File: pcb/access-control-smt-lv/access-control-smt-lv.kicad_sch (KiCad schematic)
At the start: 25 parts, among them U1 ESP32-WROOM-E

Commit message: Mostly done SMT controller
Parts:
- added C1: 0.1U, Capacitor_SMD:C_1808_4520Metric_Pad1.72x2.30mm_HandSolder, symbol Device:C
- added CON_3v3, CON_5v1: Conn_01x02_Socket, Connector_PinHeader_2.54mm:PinHeader_1x02_P2.54mm_Vertical, symbol Connector:Conn_01x02_Socket
- added CON_AUX1: Conn_01x04_Socket, Connector_PinHeader_2.54mm:PinHeader_1x04_P2.54mm_Vertical, symbol Connector:Conn_01x04_Socket
- added R_EN1: 10kR, Resistor_SMD:R_2010_5025Metric_Pad1.40x2.65mm_HandSolder, symbol Device:R
- PAD_SWL1, PAD_SWS1: footprint Connector_Wire:SolderWirePad_1x01_SMD_5x10mm -> Connector_Wire:SolderWirePad_1x01_SMD_1x2mm
- R_BUTTON_PD1: footprint Resistor_SMD:R_2816_7142Metric_Pad3.20x4.45mm_HandSolder -> Resistor_SMD:R_2010_5025Metric_Pad1.40x2.65mm_HandSolder
- R_LED1: renamed from R_LED; footprint Resistor_SMD:R_2816_7142Metric_Pad3.20x4.45mm_HandSolder -> Resistor_SMD:R_2010_5025Metric_Pad1.40x2.65mm_HandSolder
- R_Q_LED1: renamed from R_Q_LED; footprint Resistor_SMD:R_2816_7142Metric_Pad3.20x4.45mm_HandSolder -> Resistor_SMD:R_2010_5025Metric_Pad1.40x2.65mm_HandSolder
- R_Q_RELAY1: renamed from R_Q_RELAY; footprint Resistor_SMD:R_2816_7142Metric_Pad3.20x4.45mm_HandSolder -> Resistor_SMD:R_2010_5025Metric_Pad1.40x2.65mm_HandSolder
- renumbered C_PWR_5V to C_PWR_5V1, D_Z_5V to D_Z_5V1, J_LED to J_LED1, J_NFC to J_NFC1, J_RELAY to J_RELAY1, J_SERIAL to J_SERIAL1, Q_LED to Q_LED1, Q_RELAY to Q_RELAY1, SW_BOOT to SW_BOOT1, SW_RESET to SW_RESET1
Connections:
- net +3V3: now also CON_3v3.1 (Pin_1), CON_AUX1.1 (Pin_1), R_EN1.1
- net +5V: now also CON_5v1.1 (Pin_1)
- net GND: now also C1.2, CON_3v3.2 (Pin_2), CON_5v1.2 (Pin_2), CON_AUX1.2 (Pin_2)
- net at SW_RESET1.2, U1.3 (EN/CHIP_PU): now also C1.1, R_EN1.2
- net at U1.8 (32K_XP/GPIO32/ADC1_CH4): now also CON_AUX1.4 (Pin_4)
- net at U1.9 (32K_XN/GPIO33/ADC1_CH5): now also CON_AUX1.3 (Pin_3)
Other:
- moved on the sheet: SW_RESET1

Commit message: NFC Clamp and progress with contactor interface
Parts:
- C_PWR_3v3, C_PWR_5V1: footprint Capacitor_SMD:C_1808_4520Metric_Pad1.72x2.30mm_HandSolder -> Capacitor_SMD:C_1812_4532Metric_Pad1.57x3.40mm_HandSolder
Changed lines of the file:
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@@
 		(dnp no)
 		(fields_autoplaced yes)
-		(property "Reference" "#PWR25"
+		(property "Reference" "#PWR025"
 			(at 49.53 106.68 0)
 			(effects
@@
 			(project ""
 				(path "/7cf59121-d90a-405f-864e-dd3e48ad3dc1"
-					(reference "#PWR25")
+					(reference "#PWR025")
 					(unit 1)
 				)
@@
 		(dnp no)
 		(fields_autoplaced yes)
-		(property "Reference" "#PWR26"
+		(property "Reference" "#PWR026"
 			(at 49.53 111.76 0)
 			(effects
@@
 			(project ""
 				(path "/7cf59121-d90a-405f-864e-dd3e48ad3dc1"
-					(reference "#PWR26")
+					(reference "#PWR026")
 					(unit 1)
 				)
@@
 			)
 		)
-		(property "Footprint" "Capacitor_SMD:C_1808_4520Metric_Pad1.72x2.30mm_HandSolder"
+		(property "Footprint" "Capacitor_SMD:C_1812_4532Metric_Pad1.57x3.40mm_HandSolder"
 			(at 47.9552 34.29 0)
 			(effects
@@
 		(dnp no)
 		(fields_autoplaced yes)
-		(property "Reference" "#PWR28"
+		(property "Reference" "#PWR028"
 			(at 44.45 62.23 0)
 			(effects
@@
 			(project "access-control-smt-lv"
 				(path "/7cf59121-d90a-405f-864e-dd3e48ad3dc1"
-					(reference "#PWR28")
+					(reference "#PWR028")
 					(unit 1)
 				)
@@
 			)
 		)
-		(property "Footprint" "Capacitor_SMD:C_1808_4520Metric_Pad1.72x2.30mm_HandSolder"
+		(property "Footprint" "Capacitor_SMD:C_1812_4532Metric_Pad1.57x3.40mm_HandSolder"
 			(at 17.4752 34.29 0)
 			(effects
@@
 		(dnp no)
 		(fields_autoplaced yes)
-		(property "Reference" "#PWR29"
+		(property "Reference" "#PWR029"
 			(at 77.47 121.92 0)
 			(effects
@@
 			(project "access-control-smt-lv"
 				(path "/7cf59121-d90a-405f-864e-dd3e48ad3dc1"
-					(reference "#PWR29")
+					(reference "#PWR029")
 					(unit 1)
 				)
@@
 		(dnp no)
 		(fields_autoplaced yes)
-		(property "Reference" "#PWR30"
+		(property "Reference" "#PWR030"
 			(at 77.47 128.27 0)
 			(effects
@@
 			(project "access-control-smt-lv"
 				(path "/7cf59121-d90a-405f-864e-dd3e48ad3dc1"
-					(reference "#PWR30")
+					(reference "#PWR030")
 					(unit 1)
 				)
@@
 		(dnp no)
 		(fields_autoplaced yes)
-		(property "Reference" "#PWR27"
+		(property "Reference" "#PWR027"
 			(at 39.37 67.31 0)
 			(effects
@@
 			(project "access-control-smt-lv"
 				(path "/7cf59121-d90a-405f-864e-dd3e48ad3dc1"
-					(reference "#PWR27")
+					(reference "#PWR027")
 					(unit 1)
 				)
@@
 		(dnp no)
 		(fields_autoplaced yes)
-		(property "Reference" "#PWR24"
+		(property "Reference" "#PWR024"
 			(at 13.97 49.53 0)
 			(effects
@@
 			(project ""
 				(path "/7cf59121-d90a-405f-864e-dd3e48ad3dc1"
-					(reference "#PWR24")
-					(unit 1)
-				)
+					(reference "#PWR024")
+					(unit 1)
+				)

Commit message: Further optimisation of SMT version
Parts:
- C3: footprint Capacitor_SMD:C_1808_4520Metric_Pad1.72x2.30mm_HandSolder -> Capacitor_SMD:C_1206_3216Metric_Pad1.33x1.80mm_HandSolder
- C_PWR_3v3, C_PWR_5V1: footprint Capacitor_SMD:C_1812_4532Metric_Pad1.57x3.40mm_HandSolder -> Capacitor_SMD:C_1206_3216Metric_Pad1.33x1.80mm_HandSolder
- D_Z_3v3: footprint Diode_SMD:D_1210_3225Metric_Pad1.42x2.65mm_HandSolder -> Diode_SMD:D_0805_2012Metric_Pad1.15x1.40mm_HandSolder
- D_Z_5V1: footprint Diode_SMD:D_1210_3225Metric_Pad1.42x2.65mm_HandSolder -> Diode_SMD:D_1206_3216Metric_Pad1.42x1.75mm_HandSolder
- R_BUTTON_PD1, R_EN1, R_LED1, R_Q_LED1, R_Q_RELAY1: footprint Resistor_SMD:R_2010_5025Metric_Pad1.40x2.65mm_HandSolder -> Resistor_SMD:R_1206_3216Metric_Pad1.30x1.75mm_HandSolder
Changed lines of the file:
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@@
 			)
 		)
-		(property "Footprint" "Resistor_SMD:R_2010_5025Metric_Pad1.40x2.65mm_HandSolder"
+		(property "Footprint" "Resistor_SMD:R_1206_3216Metric_Pad1.30x1.75mm_HandSolder"
 			(at 163.322 31.75 90)
 			(effects
@@
 			)
 		)
-		(property "Footprint" "Capacitor_SMD:C_1812_4532Metric_Pad1.57x3.40mm_HandSolder"
+		(property "Footprint" "Capacitor_SMD:C_1206_3216Metric_Pad1.33x1.80mm_HandSolder"
 			(at 47.9552 34.29 0)
 			(effects
@@
 			)
 		)
-		(property "Footprint" "Capacitor_SMD:C_1812_4532Metric_Pad1.57x3.40mm_HandSolder"
+		(property "Footprint" "Capacitor_SMD:C_1206_3216Metric_Pad1.33x1.80mm_HandSolder"
 			(at 17.4752 34.29 0)
 			(effects
@@
 			)
 		)
-		(property "Footprint" "Resistor_SMD:R_2010_5025Metric_Pad1.40x2.65mm_HandSolder"
+		(property "Footprint" "Resistor_SMD:R_1206_3216Metric_Pad1.30x1.75mm_HandSolder"
 			(at 12.192 52.07 90)
 			(effects
@@
 			)
 		)
-		(property "Footprint" "Capacitor_SMD:C_1808_4520Metric_Pad1.72x2.30mm_HandSolder"
+		(property "Footprint" "Capacitor_SMD:C_1206_3216Metric_Pad1.33x1.80mm_HandSolder"
 			(at 68.2752 30.48 0)
 			(effects
@@
 			)
 		)
-		(property "Footprint" "Resistor_SMD:R_2010_5025Metric_Pad1.40x2.65mm_HandSolder"
+		(property "Footprint" "Resistor_SMD:R_1206_3216Metric_Pad1.30x1.75mm_HandSolder"
 			(at 190.5 109.728 90)
 			(effects
@@
 			)
 		)
-		(property "Footprint" "Resistor_SMD:R_2010_5025Metric_Pad1.40x2.65mm_HandSolder"
+		(property "Footprint" "Resistor_SMD:R_1206_3216Metric_Pad1.30x1.75mm_HandSolder"
 			(at 190.5 62.738 90)
 			(effects
@@
 			)
 		)
-		(property "Footprint" "Diode_SMD:D_1210_3225Metric_Pad1.42x2.65mm_HandSolder"
+		(property "Footprint" "Diode_SMD:D_0805_2012Metric_Pad1.15x1.40mm_HandSolder"
 			(at 105.41 30.48 0)
 			(effects
@@
 			)
 		)
-		(property "Footprint" "Diode_SMD:D_1210_3225Metric_Pad1.42x2.65mm_HandSolder"
+		(property "Footprint" "Diode_SMD:D_1206_3216Metric_Pad1.42x1.75mm_HandSolder"
 			(at 22.86 30.48 0)
 			(effects
@@
 			)
 		)
-		(property "Footprint" "Resistor_SMD:R_2010_5025Metric_Pad1.40x2.65mm_HandSolder"
+		(property "Footprint" "Resistor_SMD:R_1206_3216Metric_Pad1.30x1.75mm_HandSolder"
 			(at 218.44 56.388 90)
 			(effects

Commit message: SMT PCB Updates
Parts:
- added CON_5v2: Conn_01x02_Socket, Connector_PinHeader_2.54mm:PinHeader_1x02_P2.54mm_Vertical, symbol Connector:Conn_01x02_Socket
- added R_PRGM_SERIAL1: 10kR, Resistor_SMD:R_1206_3216Metric_Pad1.30x1.75mm_HandSolder, symbol Device:R
- C1: footprint Capacitor_SMD:C_1808_4520Metric_Pad1.72x2.30mm_HandSolder -> Capacitor_SMD:C_1206_3216Metric_Pad1.33x1.80mm_HandSolder
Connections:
- net +5V: now also CON_5v2.1 (Pin_1)
- net GND: now also CON_5v2.2 (Pin_2), R_PRGM_SERIAL1.2
- net at U1.24 (ADC2_CH2/GPIO2): now also R_PRGM_SERIAL1.1

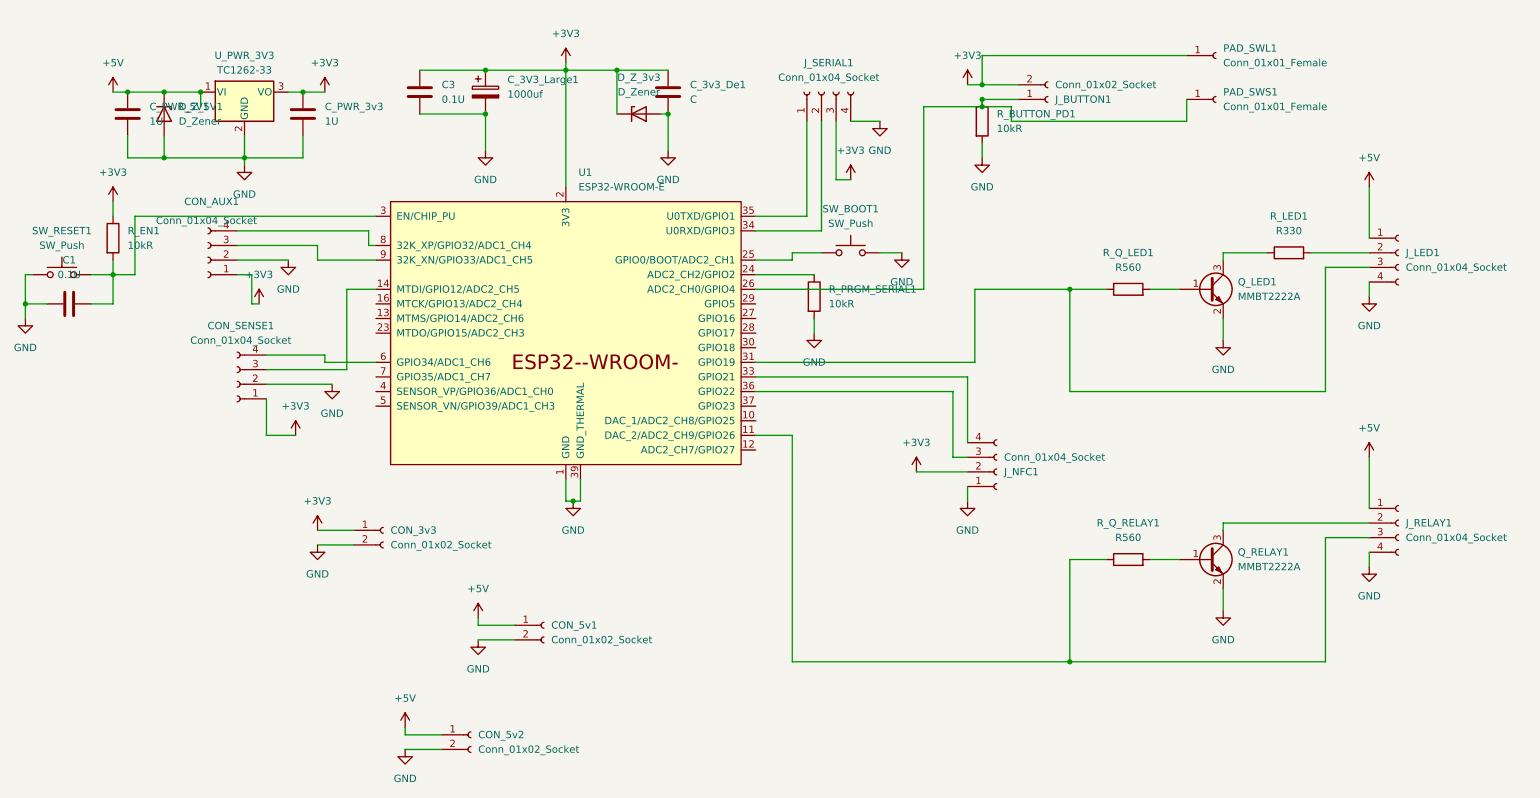
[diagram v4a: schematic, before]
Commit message: Fixes to relief, JST connectors for SMT board
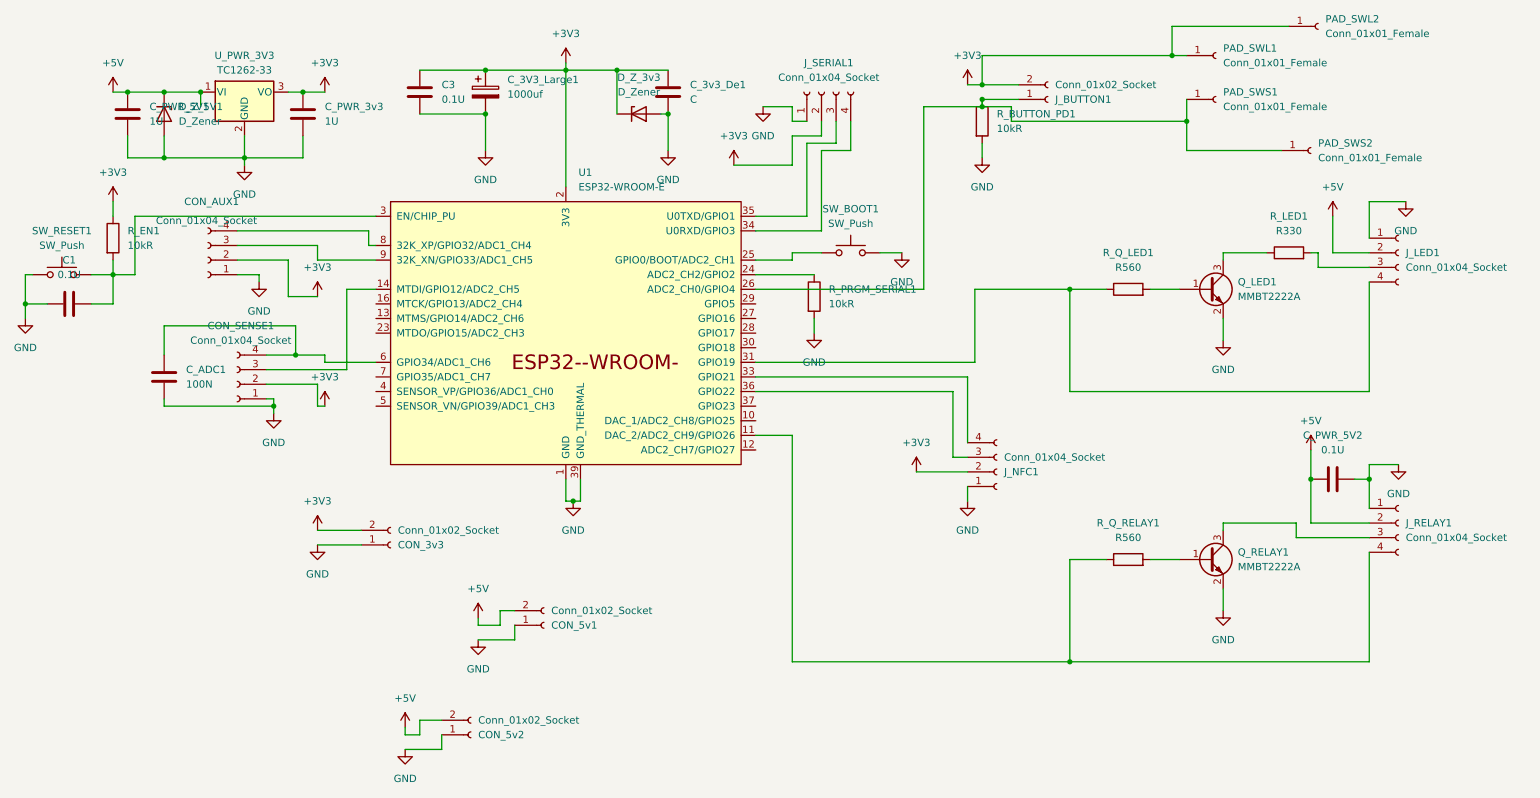
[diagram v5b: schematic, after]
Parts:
- added C_ADC1: 100N, Capacitor_SMD:C_1206_3216Metric_Pad1.33x1.80mm_HandSolder, symbol Device:C
- added C_PWR_5V2: 0.1U, Capacitor_SMD:C_1206_3216Metric_Pad1.33x1.80mm_HandSolder, symbol Device:C
- added PAD_SWL2, PAD_SWS2: Conn_01x01_Female, Connector_Wire:SolderWirePad_1x01_SMD_1x2mm, symbol Connector:Conn_01x01_Female
- CON_5v2: footprint Connector_PinHeader_2.54mm:PinHeader_1x02_P2.54mm_Vertical -> Connector_JST:JST_XH_B2B-XH-A_1x02_P2.50mm_Vertical
- CON_SENSE1: footprint Connector_PinHeader_2.54mm:PinHeader_1x04_P2.54mm_Vertical -> Connector_JST:JST_XH_B4B-XH-A_1x04_P2.50mm_Vertical
- J_NFC1, J_RELAY1, J_SERIAL1: footprint Connector_PinSocket_2.54mm:PinSocket_1x04_P2.54mm_Vertical -> Connector_JST:JST_XH_B4B-XH-A_1x04_P2.50mm_Vertical
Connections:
- net +3V3: now also CON_3v3.2 (Pin_2), CON_AUX1.2 (Pin_2), CON_SENSE1.2 (Pin_2), J_SERIAL1.2 (Pin_2), PAD_SWL2.1 (Pin_1); no longer CON_3v3.1 (Pin_1), CON_AUX1.1 (Pin_1), CON_SENSE1.1 (Pin_1), J_SERIAL1.3 (Pin_3)
- net +5V: now also CON_5v1.2 (Pin_2), CON_5v2.2 (Pin_2), J_LED1.2 (Pin_2), J_RELAY1.2 (Pin_2), C_PWR_5V2.1; no longer CON_5v1.1 (Pin_1), CON_5v2.1 (Pin_1), J_LED1.1 (Pin_1), J_RELAY1.1 (Pin_1)
- net GND: now also CON_3v3.1 (Pin_1), CON_5v1.1 (Pin_1), CON_5v2.1 (Pin_1), CON_AUX1.1 (Pin_1), CON_SENSE1.1 (Pin_1), J_LED1.1 (Pin_1), J_RELAY1.1 (Pin_1), J_SERIAL1.1 (Pin_1), C_ADC1.2, C_PWR_5V2.2; no longer CON_3v3.2 (Pin_2), CON_5v1.2 (Pin_2), CON_5v2.2 (Pin_2), CON_AUX1.2 (Pin_2), CON_SENSE1.2 (Pin_2), J_LED1.4 (Pin_4), J_RELAY1.4 (Pin_4), J_SERIAL1.4 (Pin_4)
- net at J_BUTTON1.1 (Pin_1), PAD_SWS1.1 (Pin_1), R_BUTTON_PD1.1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: now also PAD_SWS2.1 (Pin_1)
- net at CON_SENSE1.4 (Pin_4), U1.6 (GPIO34/ADC1_CH6): now also C_ADC1.1
- net at Q_RELAY1.3 (C): now also J_RELAY1.3 (Pin_3); no longer J_RELAY1.2 (Pin_2)
- net at U1.35 (U0TXD/GPIO1): now also J_SERIAL1.3 (Pin_3); no longer J_SERIAL1.1 (Pin_1)
- net at U1.34 (U0RXD/GPIO3): now also J_SERIAL1.4 (Pin_4); no longer J_SERIAL1.2 (Pin_2)
- net at R_Q_RELAY1.1, U1.11 (DAC_2/ADC2_CH9/GPIO26): now also J_RELAY1.4 (Pin_4); no longer J_RELAY1.3 (Pin_3)
- net at R_Q_LED1.1, U1.31 (GPIO19): now also J_LED1.4 (Pin_4); no longer J_LED1.3 (Pin_3)
- net at R_LED1.2: now also J_LED1.3 (Pin_3); no longer J_LED1.2 (Pin_2)
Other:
- moved on the sheet: CON_3v3, CON_5v1, CON_5v2

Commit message: Silkscreen updates with version, date and logo
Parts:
- renumbered CON_5v2 to CON_5v1, J_NFC1 to CON_NFC1, J_RELAY1 to CON_RELAY1, CON_3v3 to J_3v3, CON_5v1 to J_5v1
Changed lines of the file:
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@@
 		(on_board yes)
 		(dnp no)
-		(property "Reference" "CON_3v3"
+		(property "Reference" "J_3v3"
 			(at 63.5 105.4101 0)
 			(effects
@@
 			(project ""
 				(path "/7cf59121-d90a-405f-864e-dd3e48ad3dc1"
-					(reference "CON_3v3")
+					(reference "J_3v3")
 					(unit 1)
 				)
@@
 		(on_board yes)
 		(dnp no)
-		(property "Reference" "J_NFC1"
+		(property "Reference" "CON_NFC1"
 			(at 168.91 92.7101 0)
 			(effects
@@
 			(project "access-control-smt-lv"
 				(path "/7cf59121-d90a-405f-864e-dd3e48ad3dc1"
-					(reference "J_NFC1")
+					(reference "CON_NFC1")
 					(unit 1)
 				)
@@
 		(on_board yes)
 		(dnp no)
-		(property "Reference" "CON_5v1"
+		(property "Reference" "J_5v1"
 			(at 90.17 119.3801 0)
 			(effects
@@
 			(project "access-control-smt-lv"
 				(path "/7cf59121-d90a-405f-864e-dd3e48ad3dc1"
-					(reference "CON_5v1")
+					(reference "J_5v1")
 					(unit 1)
 				)
@@
 		(on_board yes)
 		(dnp no)
-		(property "Reference" "CON_5v2"
+		(property "Reference" "CON_5v1"
 			(at 77.47 138.4301 0)
 			(effects
@@
 			(project "access-control-smt-lv"
 				(path "/7cf59121-d90a-405f-864e-dd3e48ad3dc1"
-					(reference "CON_5v2")
+					(reference "CON_5v1")
 					(unit 1)
 				)
@@
 		(dnp no)
 		(fields_autoplaced yes)
-		(property "Reference" "J_RELAY1"
+		(property "Reference" "CON_RELAY1"
 			(at 238.76 101.5999 0)
 			(effects
@@
 			(project ""
 				(path "/7cf59121-d90a-405f-864e-dd3e48ad3dc1"
-					(reference "J_RELAY1")
+					(reference "CON_RELAY1")
 					(unit 1)
 				)

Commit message: Final changes pre manufacture
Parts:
- added R_I2C_PU1, R_I2C_PU2: 10kR, Resistor_SMD:R_1206_3216Metric_Pad1.30x1.75mm_HandSolder, symbol Device:R
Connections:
- net +3V3: now also R_I2C_PU1.2, R_I2C_PU2.2
- net at CON_NFC1.3 (Pin_3), U1.36 (GPIO22): now also R_I2C_PU1.1
- net at CON_NFC1.4 (Pin_4), U1.33 (GPIO21): now also R_I2C_PU2.1
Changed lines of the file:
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@@
 	)
 	(junction
+		(at 137.16 76.2)
+		(diameter 0)
+		(color 0 0 0 0)
+	)
+	(junction
 		(at 200.66 31.75)
 		(diameter 0)
@@
 	)
 	(junction
+		(at 144.78 92.71)
+		(diameter 0)
+		(color 0 0 0 0)
+	)
+	(junction
 		(at 198.12 20.32)
 		(diameter 0)
@@
 	)
 	(junction
+		(at 144.78 78.74)
+		(diameter 0)
+		(color 0 0 0 0)
+	)
+	(junction
 		(at 92.71 22.86)
 		(diameter 0)
@@
 	)
 	(junction
+		(at 137.16 92.71)
+		(diameter 0)
+		(color 0 0 0 0)
+	)
+	(junction
 		(at 222.25 93.98)
 		(diameter 0)
@@
 	(wire
 		(pts
+			(xy 137.16 76.2) (xy 162.56 76.2)
+		)
+		(stroke
+			(width 0)
+			(type default)
+		)
+	)
+	(wire
+		(pts
 			(xy 49.53 62.23) (xy 44.45 62.23)
 		)
@@
 	(wire
 		(pts
+			(xy 144.78 92.71) (xy 162.56 92.71)
+		)
+		(stroke
+			(width 0)
+			(type default)
+		)
+	)
+	(wire
+		(pts
 			(xy 22.86 81.28) (xy 41.91 81.28)
 		)
@@
 	(wire
 		(pts
-			(xy 125.73 86.36) (xy 132.08 86.36)
+			(xy 125.73 86.36) (xy 129.54 86.36)
 		)
 		(stroke
@@
 	(wire
 		(pts
+			(xy 137.16 92.71) (xy 144.78 92.71)
+		)
+		(stroke
+			(width 0)
+			(type default)
+		)
+	)
+	(wire
+		(pts
 			(xy 101.6 30.48) (xy 101.6 22.86)
 		)
@@
 	(wire
 		(pts
-			(xy 125.73 76.2) (xy 162.56 76.2)
+			(xy 125.73 76.2) (xy 137.16 76.2)
 		)
 		(stroke
@@
 	(wire
 		(pts
-			(xy 132.08 125.73) (xy 180.34 125.73)
+			(xy 144.78 78.74) (xy 160.02 78.74)
+		)
+		(stroke
+			(width 0)
+			(type default)
+		)
+	)
+	(wire
+		(pts
+			(xy 129.54 125.73) (xy 180.34 125.73)
 		)
 		(stroke
@@
 	(wire
 		(pts
-			(xy 132.08 86.36) (xy 132.08 125.73)
+			(xy 129.54 86.36) (xy 129.54 125.73)
 		)
 		(stroke
@@
 	(wire
 		(pts
-			(xy 153.67 92.71) (xy 162.56 92.71)
+			(xy 134.62 92.71) (xy 137.16 92.71)
 		)
 		(stroke
@@
 	(wire
 		(pts
+			(xy 137.16 83.82) (xy 137.16 92.71)
+		)
+		(stroke
+			(width 0)
+			(type default)
+		)
+	)
+	(wire
+		(pts
 			(xy 22.86 67.31) (xy 22.86 72.39)
 		)
@@
 	(wire
 		(pts
-			(xy 125.73 78.74) (xy 160.02 78.74)
+			(xy 125.73 78.74) (xy 144.78 78.74)
 		)
 		(stroke
@@
 	(wire
 		(pts
+			(xy 144.78 86.36) (xy 144.78 92.71)
+		)
+		(stroke
+			(width 0)
+			(type default)
+		)
+	)
+	(wire
+		(pts
 			(xy 50.8 72.39) (xy 45.72 72.39)
 		)
@@
 	(symbol
 		(lib_id "power:+3V3")
-		(at 153.67 92.71 0)
+		(at 134.62 92.71 0)
 		(unit 1)
 		(exclude_from_sim no)
@@
 		(fields_autoplaced yes)
 		(property "Reference" "#PWR010"
-			(at 153.67 96.52 0)
+			(at 134.62 96.52 0)
 			(effects
 				(font
@@
 		)
 		(property "Value" "+3V3"
-			(at 153.67 87.63 0)
+			(at 134.62 87.63 0)
 			(effects
 				(font
@@
 		)
 		(property "Footprint" ""
-			(at 153.67 92.71 0)
+			(at 134.62 92.71 0)
 			(effects
 				(font
@@
 		)
 		(property "Datasheet" ""
-			(at 153.67 92.71 0)
+			(at 134.62 92.71 0)
 			(effects
 				(font
@@
 		)
 		(property "Description" "Power symbol creates a global label with name \"+3V3\""
-			(at 153.67 92.71 0)
+			(at 134.62 92.71 0)
 			(effects
 				(font
@@
 	)
 	(symbol
+		(lib_id "Device:R")
+		(at 144.78 82.55 0)
+		(unit 1)
+		(exclude_from_sim no)
+		(in_bom yes)
+		(on_board yes)
+		(dnp no)
+		(fields_autoplaced yes)
+		(property "Reference" "R_I2C_PU1"
+			(at 147.32 81.2799 0)
+			(effects
+				(font
+					(size 1.27 1.27)
+				)
+				(justify left)
+			)
+		)
+		(property "Value" "10kR"
+			(at 147.32 83.8199 0)
+			(effects
+				(font
+					(size 1.27 1.27)
+				)
+				(justify left)
+			)
+		)
+		(property "Footprint" "Resistor_SMD:R_1206_3216Metric_Pad1.30x1.75mm_HandSolder"
+			(at 143.002 82.55 90)
+			(effects
+				(font
+					(size 1.27 1.27)
+				)
+				(hide yes)
+			)
+		)
+		(property "Datasheet" "~"
+			(at 144.78 82.55 0)
+			(effects
+				(font
+					(size 1.27 1.27)
+				)
+				(hide yes)
+			)
+		)
+		(property "Description" "Resistor"
+			(at 144.78 82.55 0)
+			(effects
+				(font
+					(size 1.27 1.27)
+				)
+				(hide yes)
+			)
+		)
+		(pin "1"
+		)
+		(pin "2"
+		)
+		(instances
+			(project "access-control-smt-lv"
+				(path "/7cf59121-d90a-405f-864e-dd3e48ad3dc1"
+					(reference "R_I2C_PU1")
+					(unit 1)
+				)
+			)
+		)
+	)
+	(symbol
 		(lib_id "Transistor_BJT:MMBT2222A")
 		(at 204.47 107.95 0)
@@
 					(unit 1)
 				)
+			)
+		)
+	)
+	(symbol
+		(lib_id "Device:R")
+		(at 137.16 80.01 0)
+		(unit 1)
+		(exclude_from_sim no)
+		(in_bom yes)
+		(on_board yes)
+		(dnp no)
+		(fields_autoplaced yes)
+		(property "Reference" "R_I2C_PU2"
+			(at 139.7 78.7399 0)
+			(effects
+				(font
+					(size 1.27 1.27)
+				)
+				(justify left)
+			)
+		)
+		(property "Value" "10kR"
+			(at 139.7 81.2799 0)
+			(effects
+				(font
+					(size 1.27 1.27)
+				)
+				(justify left)
+			)
+		)
+		(property "Footprint" "Resistor_SMD:R_1206_3216Metric_Pad1.30x1.75mm_HandSolder"
+			(at 135.382 80.01 90)
+			(effects
+				(font
+					(size 1.27 1.27)
+				)
+				(hide yes)
+			)
+		)
+		(property "Datasheet" "~"
+			(at 137.16 80.01 0)
+			(effects
+				(font
+					(size 1.27 1.27)
+				)
+				(hide yes)
+			)
+		)
+		(property "Description" "Resistor"
+			(at 137.16 80.01 0)
+			(effects
+				(font
+					(size 1.27 1.27)
+				)
+				(hide yes)
+			)
+		)
+		(pin "1"
+		)
+		(pin "2"
+		)
+		(instances
+			(project "access-control-smt-lv"
+				(path "/7cf59121-d90a-405f-864e-dd3e48ad3dc1"
+					(reference "R_I2C_PU2")
+					(unit 1)
+				)
